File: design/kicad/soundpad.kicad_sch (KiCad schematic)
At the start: 31 parts, among them J1 AudioJack3, J3 AudioJack3, U1 TL072, U2 6N138M, U3 PCA9685PW

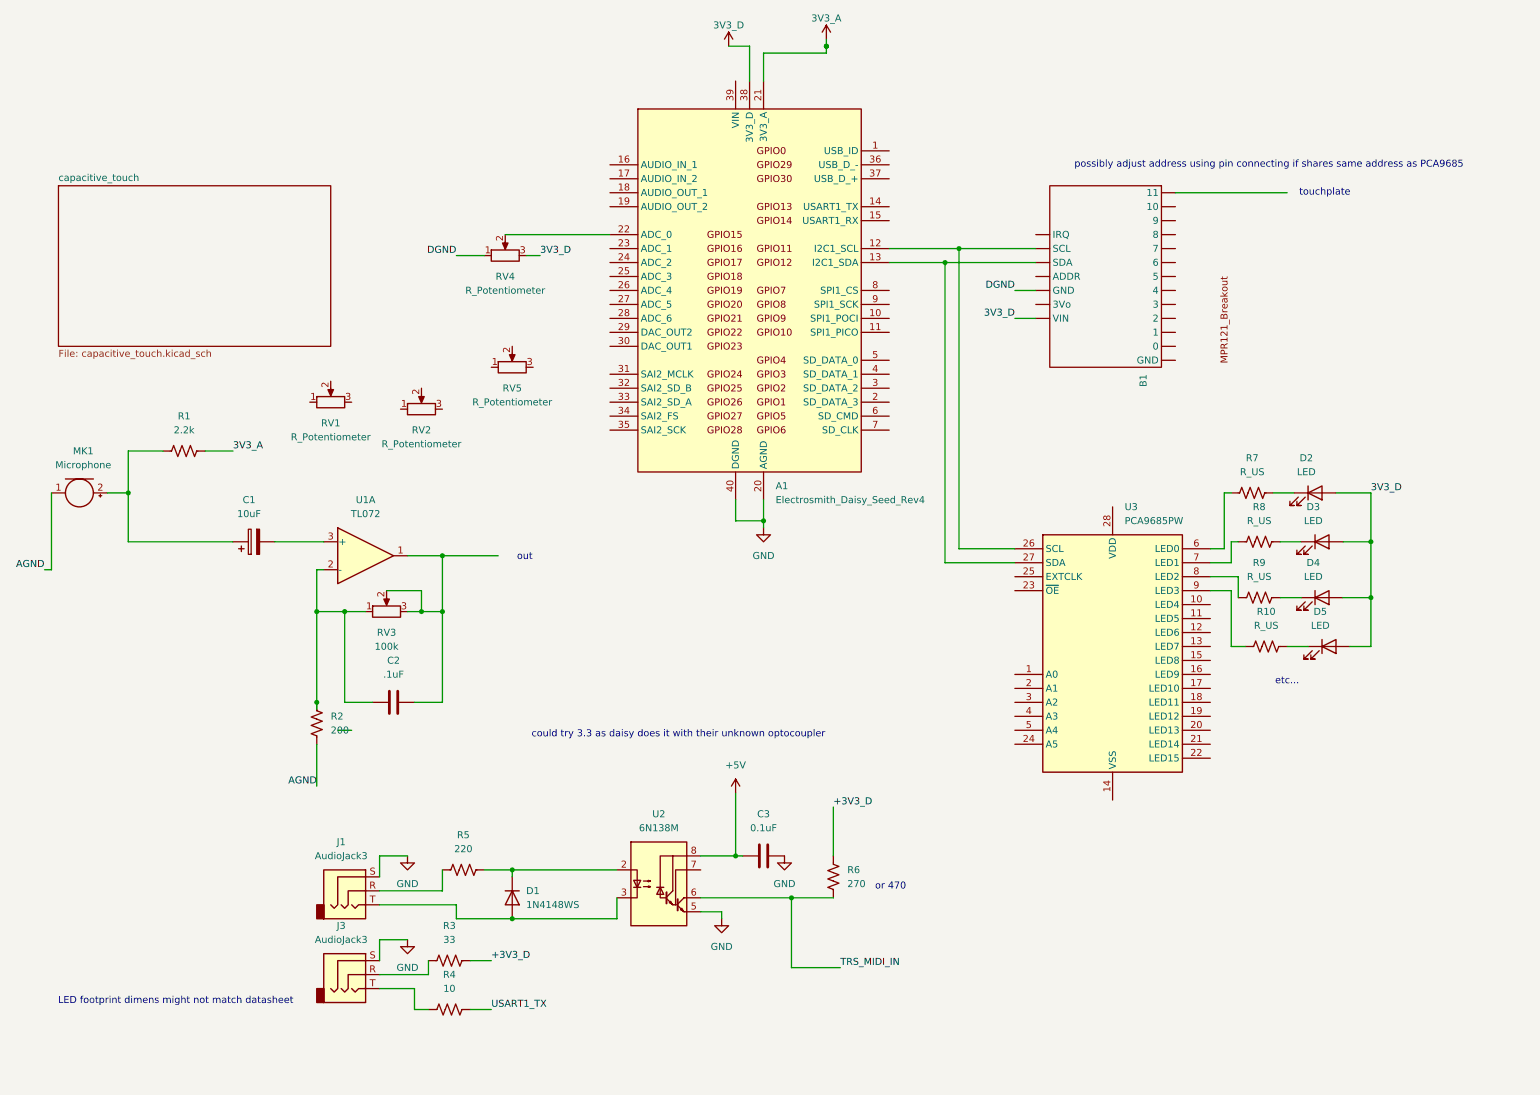
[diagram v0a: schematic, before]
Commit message: adds LEDs to design schematic
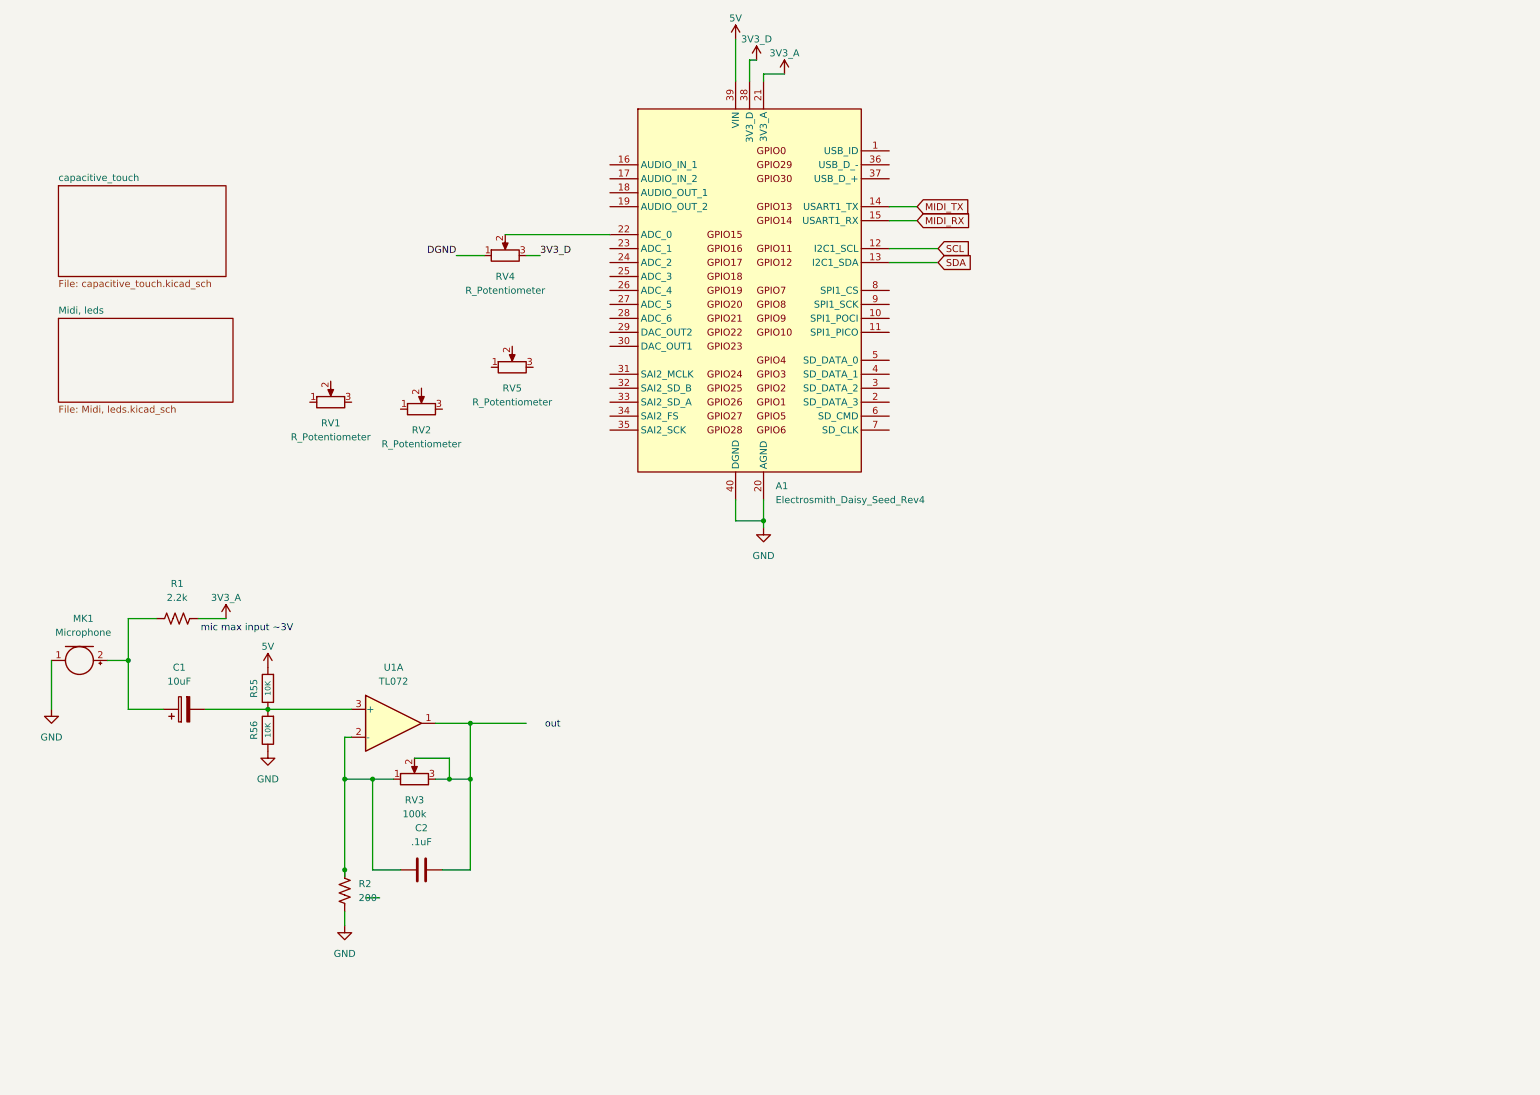
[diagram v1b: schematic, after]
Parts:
- removed B1: ~, symbol soundpad_library:Adafruit_MPR121_12-Key_Capacitive_Touch_Sensor_Breakout
- removed C3: 0.1uF, symbol Device:C
- removed D1: 1N4148WS, Diode_SMD:D_SOD-323, symbol Diode:1N4148WS
- removed D2, D3, D4, D5: LED, LED_SMD:LED_PLCC-2_3.4x3.0mm_AK, symbol Device:LED
- removed J1, J3: AudioJack3, symbol Connector_Audio:AudioJack3
- removed R10, R7, R8, R9: R_US, symbol Device:R_US
- removed R3: 33, symbol Device:R_US
- removed R4: 10, symbol Device:R_US
- removed R5: 220, symbol Device:R_US
- removed R6: 270, symbol Device:R_US
- removed U2: 6N138M, symbol Isolator:6N138
- removed U3: PCA9685PW, Package_SO:TSSOP-28_4.4x9.7mm_P0.65mm, symbol Driver_LED:PCA9685PW
- added R55, R56: 10K, Resistor_SMD:R_0603_1608Metric, symbol Device:R
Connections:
- net AGND is gone; now on net GND: MK1.1 (-), R2.1
- net GND: now also R56.1
- net at C1.2, U1.3 (+): now also R55.1, R56.2
- net SCL: now reaches A1.12 (I2C1_SCL)
- net SDA: now reaches A1.13 (I2C1_SDA)
- net MIDI_TX: now reaches A1.14 (USART1_TX)
- net MIDI_RX: now reaches A1.15 (USART1_RX)
- net 5V: now reaches A1.39 (VIN)
- net 5V: now also R55.2
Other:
- added sheet Midi, leds (Midi, leds.kicad_sch)
- note added: "mic max input ~3V"
- note removed: "LED footprint dimens might not match datasheet"
- note removed: "could try 3.3 as daisy does it with their unknown optocoupler"
- note removed: "etc..."
- note removed: "or 470"
- note removed: "possibly adjust address using pin connecting if shares same address as PCA9685"
- note removed: "touchplate"
- moved on the sheet: C1, C2, MK1, R1, R2, RV3, U1A

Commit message: completes kicad schematic, starts pcb layout
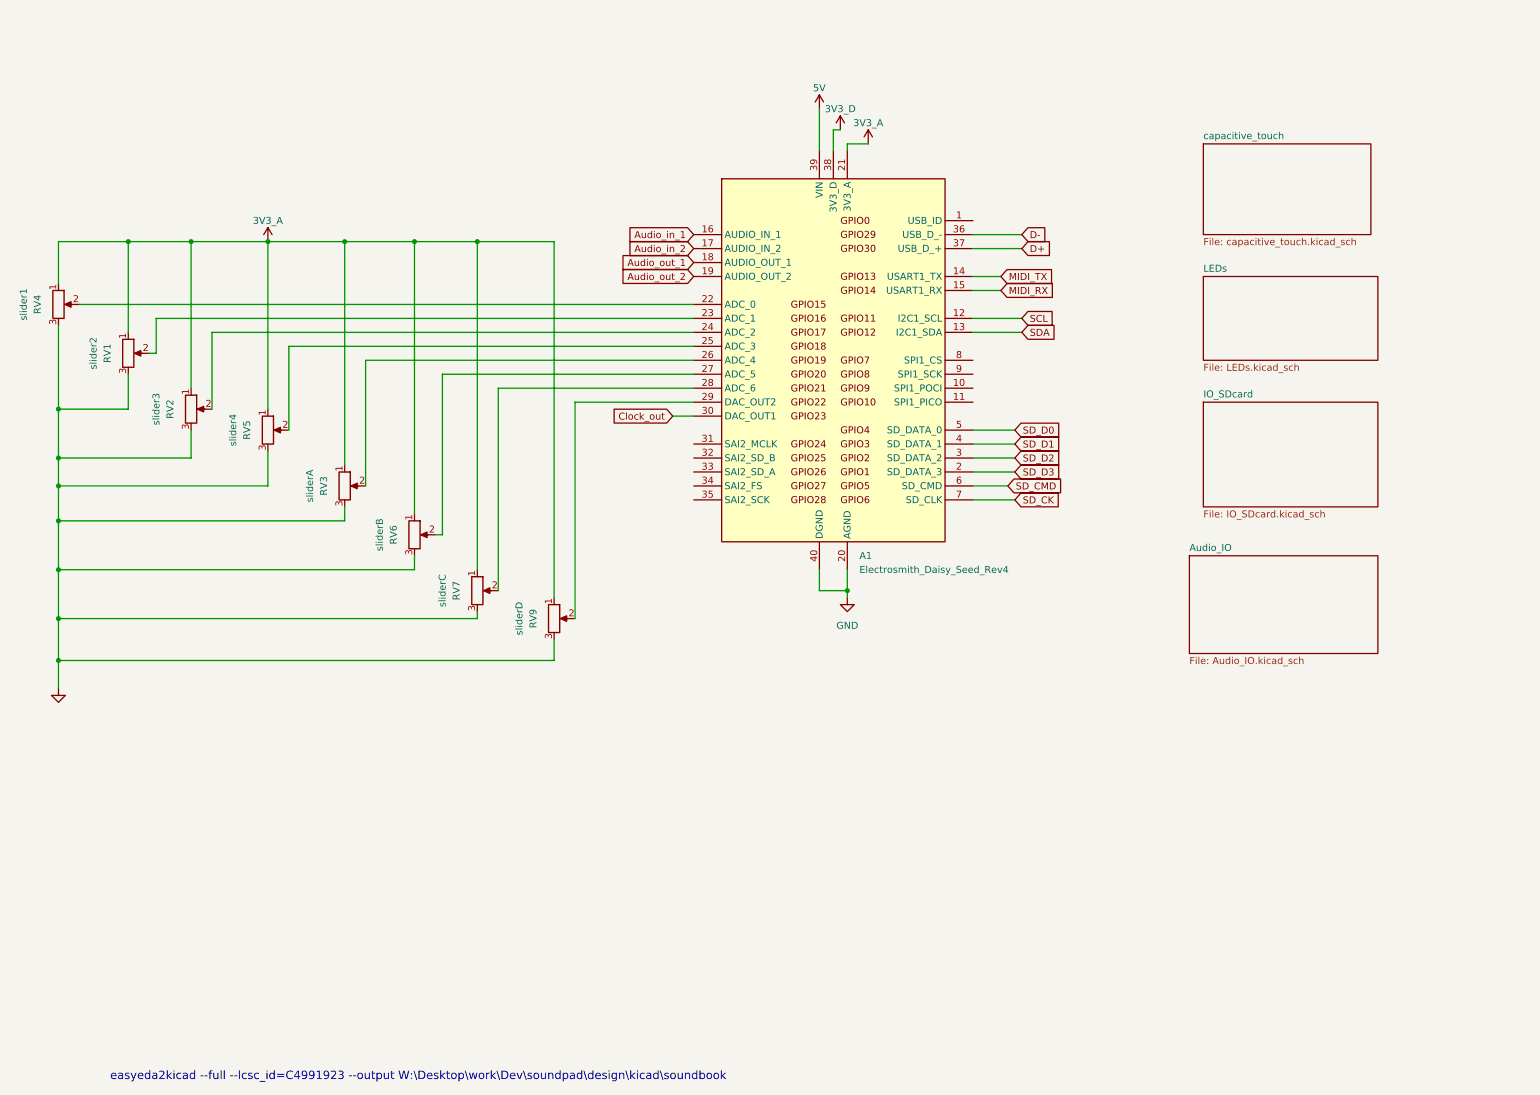
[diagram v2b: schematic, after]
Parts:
- removed C1: 10uF, symbol Device:C_Polarized
- removed C2: .1uF, symbol Device:C
- removed MK1: Microphone, symbol Device:Microphone
- removed R1: 2.2k, symbol Device:R_US
- removed R2: 200, symbol Device:R_US
- removed R55, R56: 10K, Resistor_SMD:R_0603_1608Metric, symbol Device:R
- removed U1: TL072, symbol Amplifier_Operational:TL072
- added RV6: sliderB, Potentiometer_THT:Potentiometer_Bourns_PTA4543_Single_Slide, symbol Device:R_Potentiometer
- added RV7: sliderC, Potentiometer_THT:Potentiometer_Bourns_PTA4543_Single_Slide, symbol Device:R_Potentiometer
- added RV9: sliderD, Potentiometer_THT:Potentiometer_Bourns_PTA4543_Single_Slide, symbol Device:R_Potentiometer
- RV1: value R_Potentiometer -> slider2; footprint (none) -> Potentiometer_THT:Potentiometer_Bourns_PTA6043_Single_Slide
- RV2: value R_Potentiometer -> slider3; footprint (none) -> Potentiometer_THT:Potentiometer_Bourns_PTA6043_Single_Slide
- RV3: value 100k -> sliderA; footprint (none) -> Potentiometer_THT:Potentiometer_Bourns_PTA4543_Single_Slide
- RV4: value R_Potentiometer -> slider1; footprint (none) -> Potentiometer_THT:Potentiometer_Bourns_PTA6043_Single_Slide
- RV5: value R_Potentiometer -> slider4; footprint (none) -> Potentiometer_THT:Potentiometer_Bourns_PTA6043_Single_Slide
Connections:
- net DGND is gone; now on net 3V3_A: RV4.1
- net 3V3_A: now also RV1.1, RV2.1, RV3.1, RV5.1, RV6.1, RV7.1, RV9.1
- net 3V3_D: no longer RV4.3
- net GND: now also RV1.3, RV2.3, RV3.3, RV4.3, RV5.3, RV6.3, RV7.3, RV9.3
- net at RV5.2: now also A1.25 (ADC_3)
- net at RV2.2: now also A1.24 (ADC_2)
- net at RV1.2: now also A1.23 (ADC_1)
- net at RV3.2: now also A1.26 (ADC_4); no longer RV3.3
- net Audio_in_1: now reaches A1.16 (AUDIO_IN_1)
- net Audio_in_2: now reaches A1.17 (AUDIO_IN_2)
- net Audio_out_1: now reaches A1.18 (AUDIO_OUT_1)
- net Audio_out_2: now reaches A1.19 (AUDIO_OUT_2)
- net SD_D3: now reaches A1.2 (SD_DATA_3)
- net at A1.27 (ADC_5): now also RV6.2
- net at A1.28 (ADC_6): now also RV7.2
- net at A1.29 (DAC_OUT2): now also RV9.2
- net SD_D2: now reaches A1.3 (SD_DATA_2)
- net Clock_out: now reaches A1.30 (DAC_OUT1)
- net D-: now reaches A1.36 (USB_D_-)
- net D+: now reaches A1.37 (USB_D_+)
- net SD_D1: now reaches A1.4 (SD_DATA_1)
- net SD_D0: now reaches A1.5 (SD_DATA_0)
- net SD_CMD: now reaches A1.6 (SD_CMD)
- net SD_CK: now reaches A1.7 (SD_CLK)
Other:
- sheet Midi, leds renamed LEDs
- added sheet Audio_IO (Audio_IO.kicad_sch)
- added sheet IO_SDcard (IO_SDcard.kicad_sch)
- sheet LEDs: file Midi, leds.kicad_sch -> LEDs.kicad_sch
- note added: "easyeda2kicad --full --lcsc_id=C4991923 --output W:\Desktop\work\Dev\soundpad\design\kicad\soundbook"
- note removed: "mic max input ~3V"
- note removed: "out"
- moved on the sheet: A1, RV4
